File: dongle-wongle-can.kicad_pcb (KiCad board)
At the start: 2 copper layers, 29.2 x 61 mm, 36 parts, among them J1 MicroLock, J3 PROTO_PWR, J4 UART_DEBUG, J5 Conn_ARM_JTAG_SWD_10, J6 PROTO1, J7 PROTO2, SW1 SW_Push, U1 STM32F042F6Px, U2 SN65HVD233, U3 AP1509-33

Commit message: improve silk
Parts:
- added svg2mod: G***, hardware-sch-blocks:airbears, B.Cu at (161.3, 142.4)
- moved R3 0.89 mm to (146.1, 153.3)
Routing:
- net Net-(D1-Pad1): track 2.48 -> 7.99 mm
- net SWDCLK: track 47.8 -> 49.9 mm
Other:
- board text added: "G"
- board text added: "K"
- board text added: "NC"
- board text added: "RST"
- board text added: "RX"
- board text added: "SWDCLK"
- board text added: "SWDIO"
- board text added: "TX"
- board text added: "V"

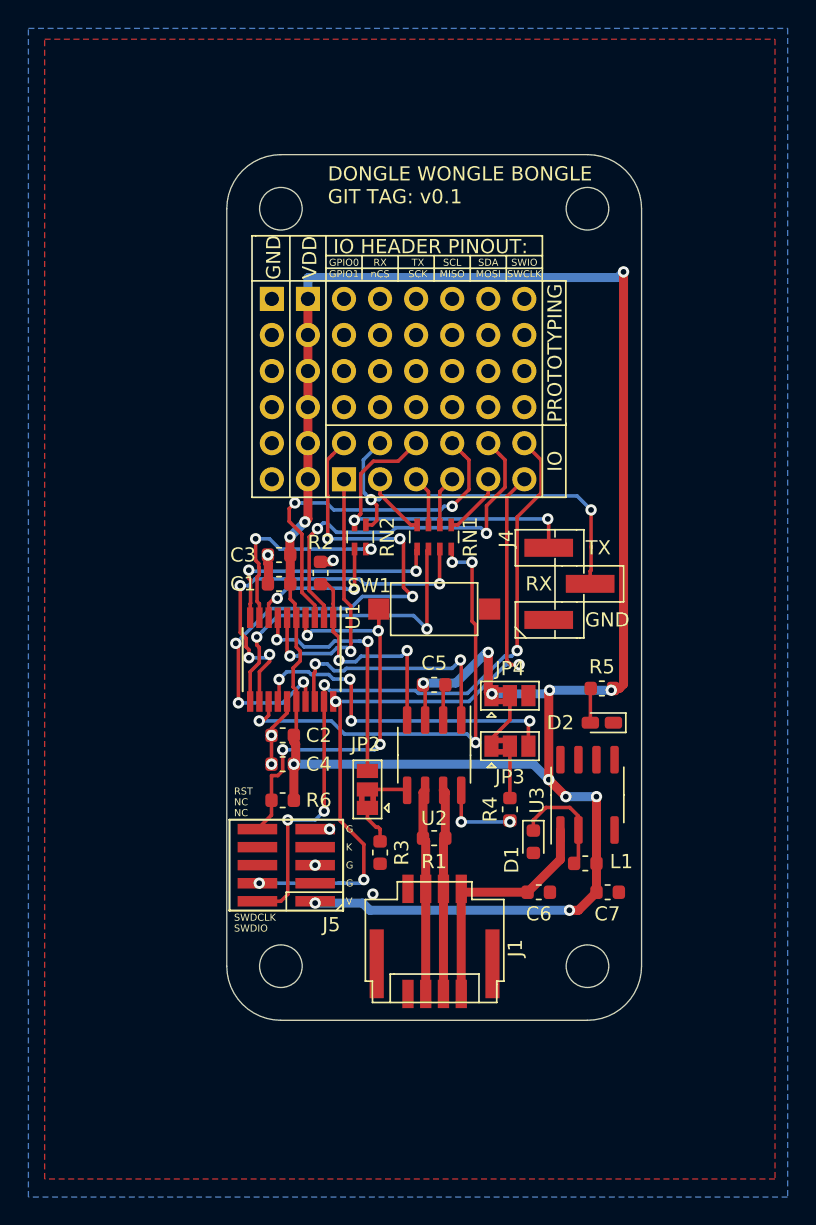
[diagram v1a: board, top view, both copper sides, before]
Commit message: make silk 10/10 and add some art
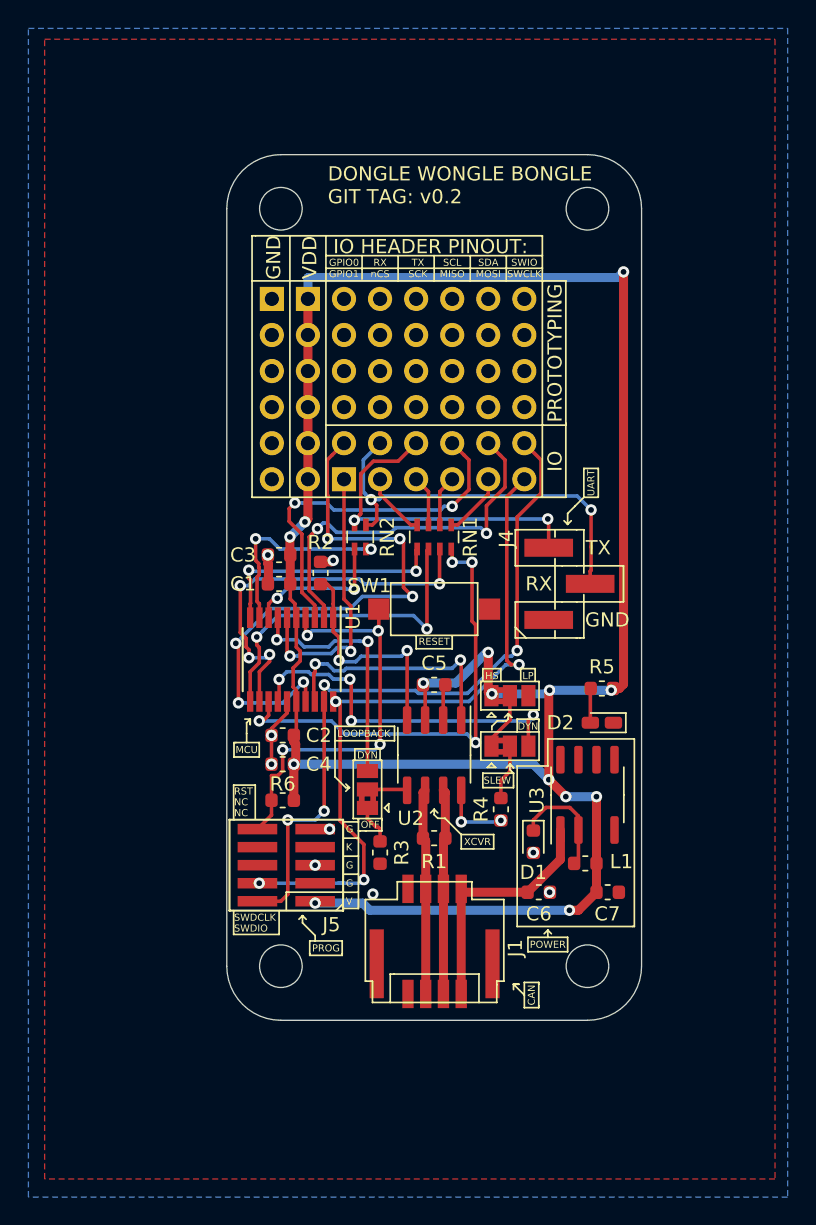
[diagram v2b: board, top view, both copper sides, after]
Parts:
- removed svg2mod: G***, hardware-sch-blocks:airbears
- added G***: LOGO, hardware-sch-blocks:star, B.Cu at (161.0, 121.2)
- added H5: Dummy Hole, hardware-sch-blocks:airbears, B.Cu at (159.6, 142.1)
- moved R4 0.63 mm to (154.6, 150.2)
- renumbered Jd to J2
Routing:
- net DYNAMIC_SLEW: track 24.4 -> 25.5 mm
- net SLEW_CTRL: track 5.75 -> 5.06 mm
- net GND: vias 7 -> 9
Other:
- board text added: "CAN"
- board text added: "C_RX"
- board text added: "C_TX"
- board text added: "DO NOT MOUNT DIRECTLY TO A METAL BULKHEAD"
- board text added: "DONGLE WONGLE BONGLE GIT TAG: v0.2"
- board text added: "DYN"
- board text added: "FUNC"
- board text added: "GPIO0"
- board text added: "GPIO1"
- board text added: "HS"
- board text added: "LOOPBACK"
- board text added: "LP"
- board text added: "MCU"
- board text added: "MISO"
- board text added: "MOSI"
- board text added: "OFF"
- board text added: "PA0"
- board text added: "PA11/9"
- board text added: "PA12/10"
- board text added: "PA13"
- board text added: "PA14"
- board text added: "PA2"
- board text added: "PA3"
- board text added: "PA4"
- board text added: "PA5"
- board text added: "PA6"
- board text added: "PA7"
- board text added: "PB8"
- board text added: "PF0"
- board text added: "PF1"
- board text added: "POWER"
- board text added: "PROG"
- board text added: "PROPERTY OF SPACE TECHNOLOGIES AND ROCKETRY UC BERKELEY"
- board text added: "RESET"
- board text added: "SCK"
- board text added: "SCL"
- board text added: "SCLK"
- board text added: "SDA"
- board text added: "SLEW"
- board text added: "STM PIN"
- board text added: "UART"
- board text added: "XCVR"
- board text added: "ld;cd"
- board text added: "nCS"
- board text removed: "DONGLE WONGLE BONGLE GIT TAG: v0.1"

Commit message: forgot to refill zones, like a dumbass
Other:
- board text added: "DONGLE WONGLE BONGLE GIT TAG: v0.2.1"
- board text removed: "DONGLE WONGLE BONGLE GIT TAG: v0.2"
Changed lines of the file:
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@@
       (outputformat 1)
       (mirror false)
-      (drillshape 1)
+      (drillshape 0)
       (scaleselection 1)
-      (outputdirectory ""))
+      (outputdirectory "../../../../tmp/donglewonglebongle/"))
   )
   (net 0 "")
@@
   )
   (gr_line (start 142.24 113.03) (end 142.24 123.19) (layer F.SilkS) (width 0.12))
-  (gr_text "DONGLE WONGLE BONGLE\nGIT TAG: v0.2" (at 142.367 106.299) (layer F.SilkS)
+  (gr_text "DONGLE WONGLE BONGLE\nGIT TAG: v0.2.1" (at 142.367 106.299) (layer F.SilkS)
     (effects (font (size 1 1) (thickness 0.15)) (justify left))
   )

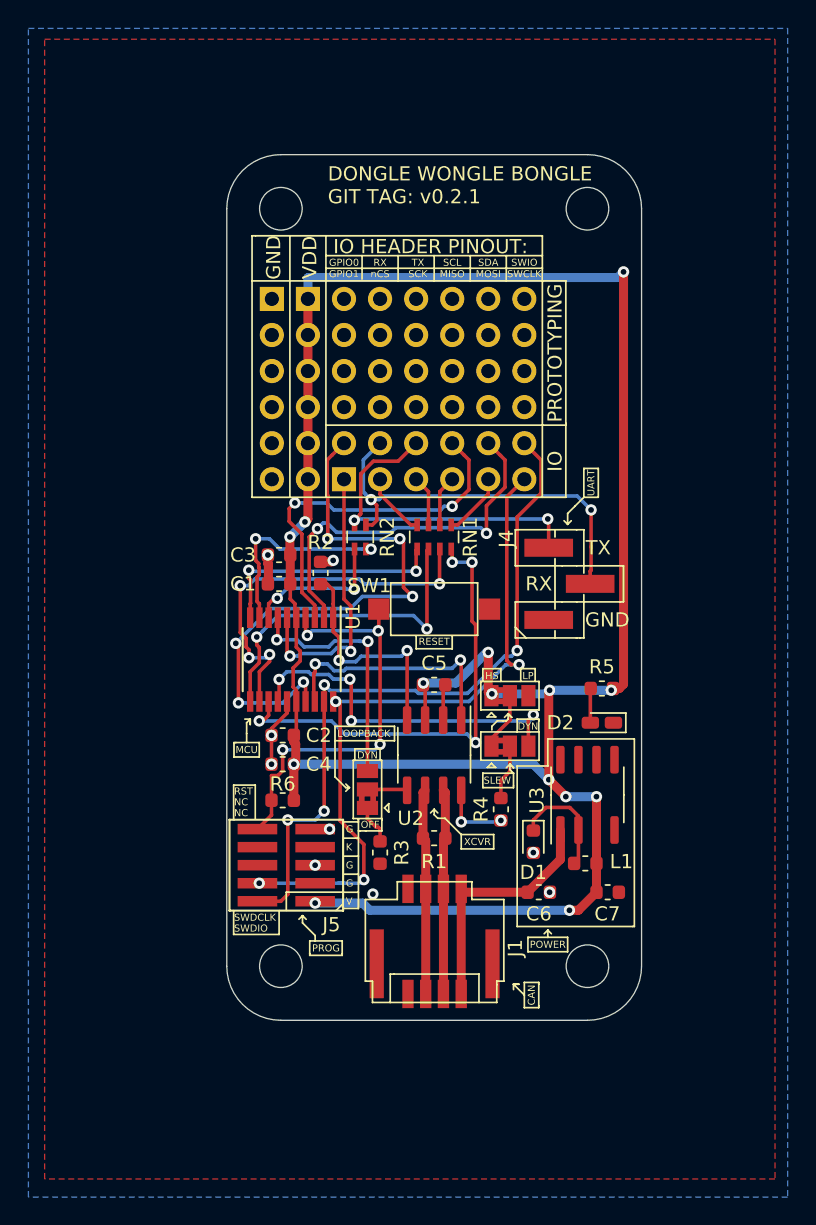
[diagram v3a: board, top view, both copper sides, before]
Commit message: increase edge cuts to make osh happy
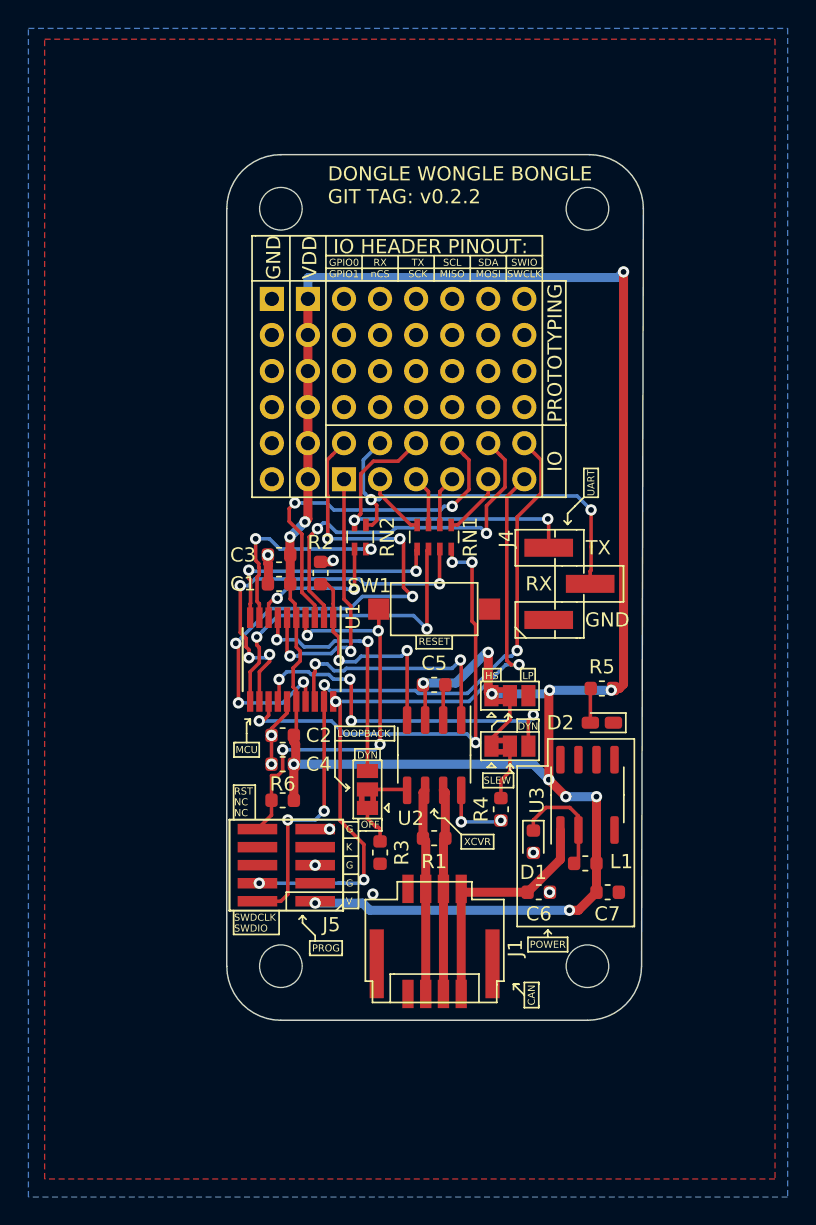
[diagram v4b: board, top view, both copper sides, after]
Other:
- board size 29.2 x 61 mm -> 29.3 x 61 mm
- board text added: "DONGLE WONGLE BONGLE GIT TAG: v0.2.2"
- board text removed: "DONGLE WONGLE BONGLE GIT TAG: v0.2.1"
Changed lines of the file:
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@@
   )
   (setup
-    (last_trace_width 0.25)
+    (last_trace_width 0.254)
     (user_trace_width 0.254)
     (user_trace_width 0.635)
@@
     )
   )
+  (gr_line (start 164.592 107.95) (end 164.465 161.29) (layer Edge.Cuts) (width 0.1016))
+  (gr_line (start 139.065 165.1) (end 160.655 165.1) (layer Edge.Cuts) (width 0.1016))
+  (gr_line (start 135.255 107.95) (end 135.255 161.29) (layer Edge.Cuts) (width 0.1016))
+  (gr_line (start 160.782 104.14) (end 139.065 104.14) (layer Edge.Cuts) (width 0.1016))
+  (gr_arc (start 160.782 107.95) (end 164.592 107.95) (angle -90) (layer Edge.Cuts) (width 0.1016))
+  (gr_arc (start 160.655 161.29) (end 160.655 165.1) (angle -90) (layer Edge.Cuts) (width 0.1016))
+  (gr_arc (start 139.065 161.29) (end 135.255 161.29) (angle -90) (layer Edge.Cuts) (width 0.1016))
+  (gr_arc (start 139.065 107.95) (end 139.065 104.14) (angle -90) (layer Edge.Cuts) (width 0.1016))
   (gr_line (start 142.24 123.19) (end 157.48 123.19) (layer B.SilkS) (width 0.12))
   (gr_line (start 157.48 113.03) (end 142.24 113.03) (layer B.SilkS) (width 0.12))
@@
   )
   (gr_line (start 142.24 113.03) (end 142.24 123.19) (layer F.SilkS) (width 0.12))
-  (gr_text "DONGLE WONGLE BONGLE\nGIT TAG: v0.2.1" (at 142.367 106.299) (layer F.SilkS)
+  (gr_text "DONGLE WONGLE BONGLE\nGIT TAG: v0.2.2" (at 142.367 106.299) (layer F.SilkS)
     (effects (font (size 1 1) (thickness 0.15)) (justify left))
   )
@@
     (effects (font (size 1 1) (thickness 0.15)))
   )
-  (gr_line (start 160.655 104.14) (end 139.065 104.14) (layer Edge.Cuts) (width 0.05))
-  (gr_line (start 164.465 161.29) (end 164.465 107.95) (layer Edge.Cuts) (width 0.05))
-  (gr_line (start 139.065 165.1) (end 160.655 165.1) (layer Edge.Cuts) (width 0.05))
-  (gr_line (start 135.255 107.95) (end 135.255 161.29) (layer Edge.Cuts) (width 0.05))
-  (gr_arc (start 160.655 107.95) (end 164.465 107.95) (angle -90) (layer Edge.Cuts) (width 0.05))
-  (gr_arc (start 139.065 107.95) (end 139.065 104.14) (angle -90) (layer Edge.Cuts) (width 0.05))
-  (gr_arc (start 160.655 161.29) (end 160.655 165.1) (angle -90) (layer Edge.Cuts) (width 0.05))
-  (gr_arc (start 139.065 161.29) (end 135.255 161.29) (angle -90) (layer Edge.Cuts) (width 0.05))
   (via (at 157.988 156.083) (size 0.8) (drill 0.4) (layers F.Cu B.Cu) (net 1))
   (via (at 156.845 153.289) (size 0.8) (drill 0.4) (layers F.Cu B.Cu) (net 1))

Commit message: stitch grounds a bit
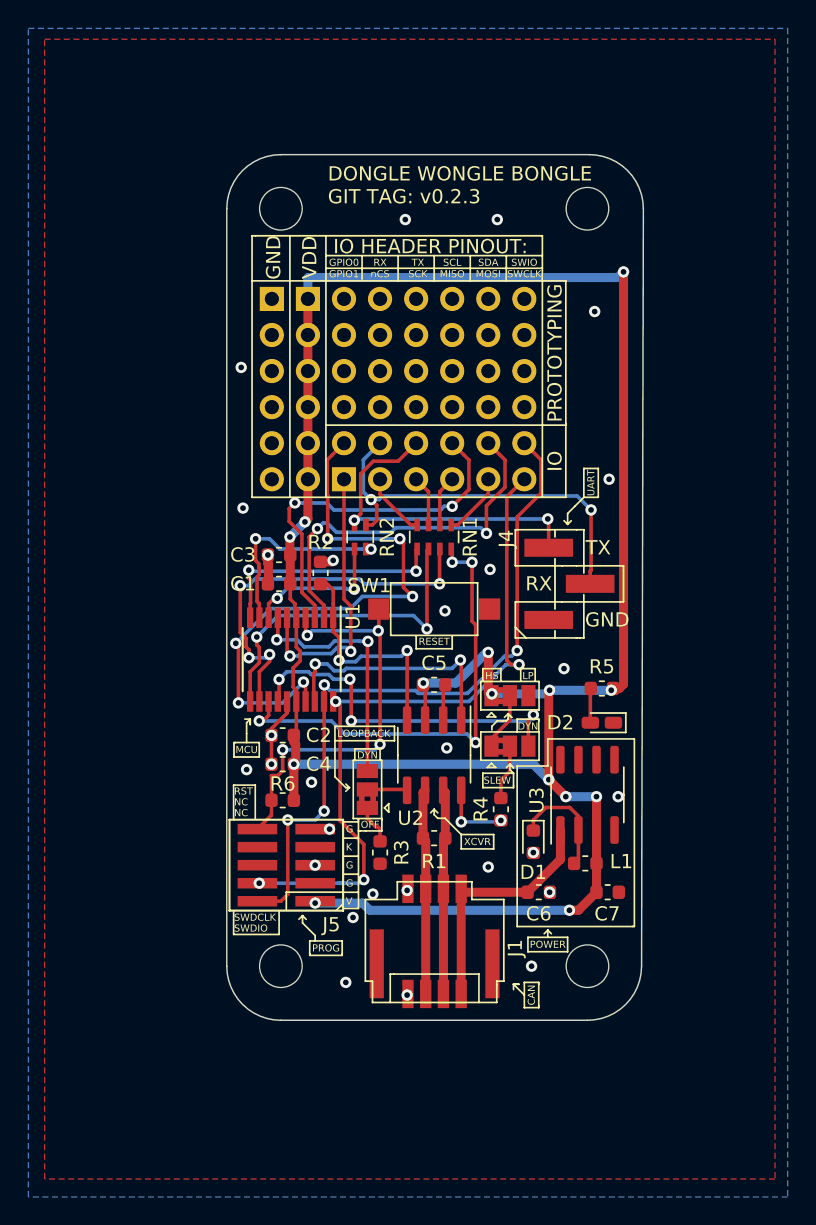
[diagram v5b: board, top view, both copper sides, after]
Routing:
- net GND: vias 9 -> 28
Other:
- board text added: "DONGLE WONGLE BONGLE GIT TAG: v0.2.3"
- board text removed: "DONGLE WONGLE BONGLE GIT TAG: v0.2.2"
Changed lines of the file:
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@@
     (thickness 1.6)
     (drawings 273)
-    (tracks 491)
+    (tracks 510)
     (zones 0)
     (modules 38)
@@
     (44 Edge.Cuts user)
     (45 Margin user)
-    (46 B.CrtYd user)
-    (47 F.CrtYd user)
-    (48 B.Fab user)
-    (49 F.Fab user)
+    (46 B.CrtYd user hide)
+    (47 F.CrtYd user hide)
+    (48 B.Fab user hide)
+    (49 F.Fab user hide)
   )
   (setup
-    (last_trace_width 0.254)
+    (last_trace_width 0.25)
     (user_trace_width 0.254)
     (user_trace_width 0.635)
@@
   )
   (gr_line (start 142.24 113.03) (end 142.24 123.19) (layer F.SilkS) (width 0.12))
-  (gr_text "DONGLE WONGLE BONGLE\nGIT TAG: v0.2.2" (at 142.367 106.299) (layer F.SilkS)
+  (gr_text "DONGLE WONGLE BONGLE\nGIT TAG: v0.2.3" (at 142.367 106.299) (layer F.SilkS)
     (effects (font (size 1 1) (thickness 0.15)) (justify left))
   )
@@
     (effects (font (size 1 1) (thickness 0.15)))
   )
+  (via (at 147.955 155.956) (size 0.8) (drill 0.4) (layers F.Cu B.Cu) (net 1))
+  (via (at 147.955 163.322) (size 0.8) (drill 0.4) (layers F.Cu B.Cu) (net 1))
   (via (at 157.988 156.083) (size 0.8) (drill 0.4) (layers F.Cu B.Cu) (net 1))
   (via (at 156.845 153.289) (size 0.8) (drill 0.4) (layers F.Cu B.Cu) (net 1))
@@
   (segment (start 141.859 132.8165) (end 142.6465 132.8165) (width 0.635) (layer F.Cu) (net 1))
   (segment (start 142.6465 132.8165) (end 142.748 132.715) (width 0.635) (layer F.Cu) (net 1))
+  (via (at 153.67 154.305) (size 0.8) (drill 0.4) (layers F.Cu B.Cu) (net 1))
+  (via (at 143.637 162.433) (size 0.8) (drill 0.4) (layers F.Cu B.Cu) (net 1))
+  (via (at 156.718 161.29) (size 0.8) (drill 0.4) (layers F.Cu B.Cu) (net 1))
+  (via (at 144.145 157.861) (size 0.8) (drill 0.4) (layers F.Cu B.Cu) (net 1))
+  (via (at 141.224 148.336) (size 0.8) (drill 0.4) (layers F.Cu B.Cu) (net 1))
+  (via (at 136.652 147.447) (size 0.8) (drill 0.4) (layers F.Cu B.Cu) (net 1))
+  (via (at 150.622 136.271) (size 0.8) (drill 0.4) (layers F.Cu B.Cu) (net 1))
+  (via (at 159.004 140.335) (size 0.8) (drill 0.4) (layers F.Cu B.Cu) (net 1))
+  (via (at 162.179 127) (size 0.8) (drill 0.4) (layers F.Cu B.Cu) (net 1))
+  (via (at 161.163 115.189) (size 0.8) (drill 0.4) (layers F.Cu B.Cu) (net 1))
+  (via (at 136.271 119.126) (size 0.8) (drill 0.4) (layers F.Cu B.Cu) (net 1))
+  (via (at 147.828 108.712) (size 0.8) (drill 0.4) (layers F.Cu B.Cu) (net 1))
+  (via (at 154.305 108.712) (size 0.8) (drill 0.4) (layers F.Cu B.Cu) (net 1))
+  (via (at 162.814 149.352) (size 0.8) (drill 0.4) (layers F.Cu B.Cu) (net 1))
+  (via (at 150.749 145.923) (size 0.8) (drill 0.4) (layers F.Cu B.Cu) (net 1))
+  (via (at 153.797 133.35) (size 0.8) (drill 0.4) (layers F.Cu B.Cu) (net 1))
+  (via (at 136.398 129.032) (size 0.8) (drill 0.4) (layers F.Cu B.Cu) (net 1))
   (segment (start 149.225 141.6305) (end 149.0725 141.478) (width 0.254) (layer F.Cu) (net 2))
   (segment (start 149.225 143.956) (end 149.225 141.6305) (width 0.254) (layer F.Cu) (net 2))

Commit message: change resistor pack footprints
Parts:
- RN1: footprint Resistor_SMD:R_Array_Concave_4x0603 -> Resistor_SMD:R_Array_Convex_4x1206
- RN2: value 200 -> 330; footprint Resistor_SMD:R_Array_Concave_2x0603 -> Resistor_SMD:R_Array_Convex_2x0606
- moved RN1 0.25 mm to (150.1, 131.1)
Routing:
- net I2C_SCL: track 25.8 -> 23.6 mm
- net SPI_SCK: track 23.6 -> 21.6 mm
- net SPI_MOSI: track 32.8 -> 30.9 mm, vias 4 -> 2
- net Net-(J2-Pad9): track 4.56 -> 3.21 mm
- net SPI_nCS: track 16.8 -> 15.7 mm
- net Net-(J2-Pad7): track 3.57 -> 2.71 mm
- net Net-(J2-Pad5): track 3.57 -> 2.92 mm
- net Net-(J2-Pad3): track 4.56 -> 3.98 mm
- net GND: vias 28 -> 26
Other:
- board text added: "DONGLE WONGLE BONGLE GIT TAG: v0.2.4"
- board text removed: "DONGLE WONGLE BONGLE GIT TAG: v0.2.3"

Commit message: implement suggested changes
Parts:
- removed JP2: Loopback Jumper, Jumper:SolderJumper-3_P1.3mm_Bridged2Bar12_Pad1.0x1.5mm
- removed JP4: Slew Jumper 2, Jumper:SolderJumper-3_P1.3mm_Bridged2Bar12_Pad1.0x1.5mm
- added F1: Fuse_Small, Fuse:Fuse_0603_1608Metric, F.Cu at (146.2, 153.1)
- added R7: 200, Resistor_SMD:R_0603_1608Metric, F.Cu at (143.5, 160.0)
- JP3: value Slew Jumper 1 -> SLEW CONTROL
- L1: footprint Inductor_SMD:L_0603_1608Metric -> Inductor_SMD:L_Bourns_SRN6045TA
- R3: value 1k -> DNP
- moved R4 13.2 mm to (145.3, 140.9), turned to 90 degrees
- moved JP3 9.95 mm to (145.3, 144.9), turned to 270 degrees
- moved C7 6.28 mm to (156.6, 159.1), turned to 270 degrees
- moved L1 5.91 mm to (159.6, 148.2)
- moved U3 5.55 mm to (159.6, 154.7), turned to 0 degrees
- moved C6 4.66 mm to (154.9, 152.0), turned to 90 degrees
- moved R3 4.66 mm to (144.7, 148.8), turned to 270 degrees
- moved D2 4.30 mm to (158.1, 141.7), turned to 0 degrees
- moved D1 3.28 mm to (154.2, 154.4), turned to 180 degrees
- moved G*** 1.28 mm to (161.2, 119.9)
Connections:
- J5 pad 1: VDD -> Net-(F1-Pad1)
- JP3 pad 2: Net-(JP3-Pad2) -> SLEW_CTRL
- JP3 pad 3: DYNAMIC_SLEW -> Net-(JP3-Pad3)
- R3 pad 1: GND -> Net-(JP3-Pad3)
- R3 pad 2: Net-(JP2-Pad1) -> DYNAMIC_SLEW
- R4 pad 1: Net-(JP3-Pad2) -> Net-(JP3-Pad1)
- R4 pad 2: SLEW_CTRL -> DYNAMIC_SLEW
- U1 pad 7: DYNAMIC_LOOPBACK -> LOOPBACK
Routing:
- net LOOPBACK: track 2.82 -> 27.4 mm, vias 0 -> 4
- net VDD: track 166.7 -> 143.4 mm, vias 14 -> 9
- net DYNAMIC_LOOPBACK: track 17.5 -> 0.00 mm, vias 2 -> 0
- net GPIO0: track 41.8 -> 55.1 mm, vias 6 -> 2
- net Net-(F1-Pad1): track 0.00 -> 8.37 mm, vias 0 -> 2
- net SPI_MOSI: track 30.9 -> 25.0 mm, vias 2 -> 4
- net SLEW_CTRL: track 5.06 -> 9.73 mm
- net SWDCLK: track 49.9 -> 54.6 mm
- net Net-(JP3-Pad2): track 3.92 -> 0.00 mm
- net GND: track 10.4 -> 13.4 mm, vias 26 -> 34
- net Net-(JP2-Pad1): track 2.81 -> 0.00 mm
- net UPOWER: track 17.5 -> 15.0 mm
- net Net-(JP3-Pad1): track 4.09 -> 1.95 mm
- net Net-(JP3-Pad3): track 0.00 -> 2.13 mm
- net DYNAMIC_SLEW: track 25.5 -> 27.5 mm, vias 4 -> 2
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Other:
- board text added: "DONGLE WONGLE BONGLE GIT TAG: v0.3"
- board text removed: "DONGLE WONGLE BONGLE GIT TAG: v0.2.4"
- board text removed: "DYN"
- board text removed: "HS"
- board text removed: "LOOPBACK"
- board text removed: "LP"
- board text removed: "OFF"
- board text removed: "SLEW"
